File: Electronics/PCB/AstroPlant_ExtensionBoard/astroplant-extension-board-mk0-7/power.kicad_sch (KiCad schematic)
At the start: 13 parts, among them J14 61300621121, J20 Conn_01x02, J21 Conn_01x02

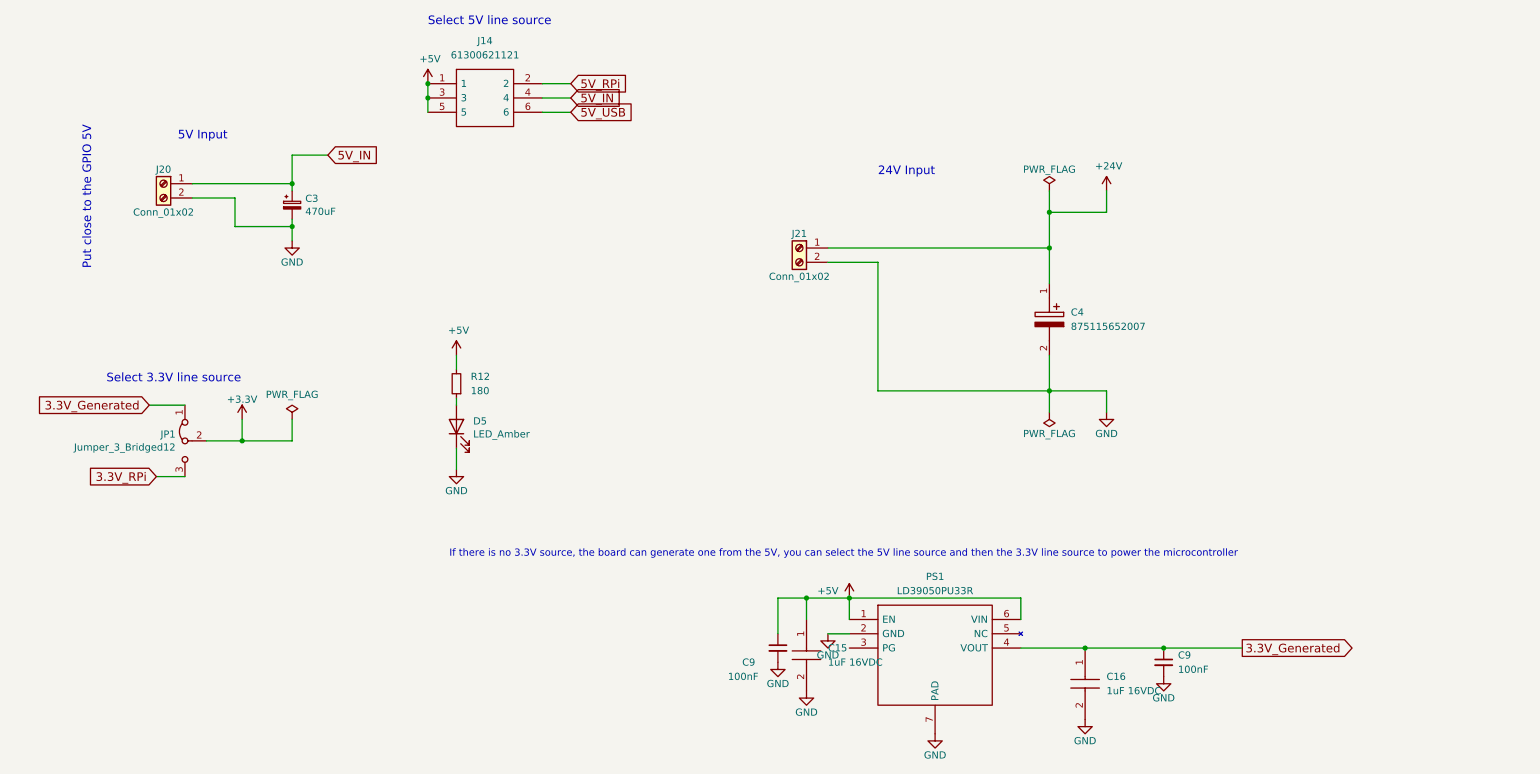
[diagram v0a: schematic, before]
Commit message: Updated PCB from a backup save, solve issues of the 1st prototype
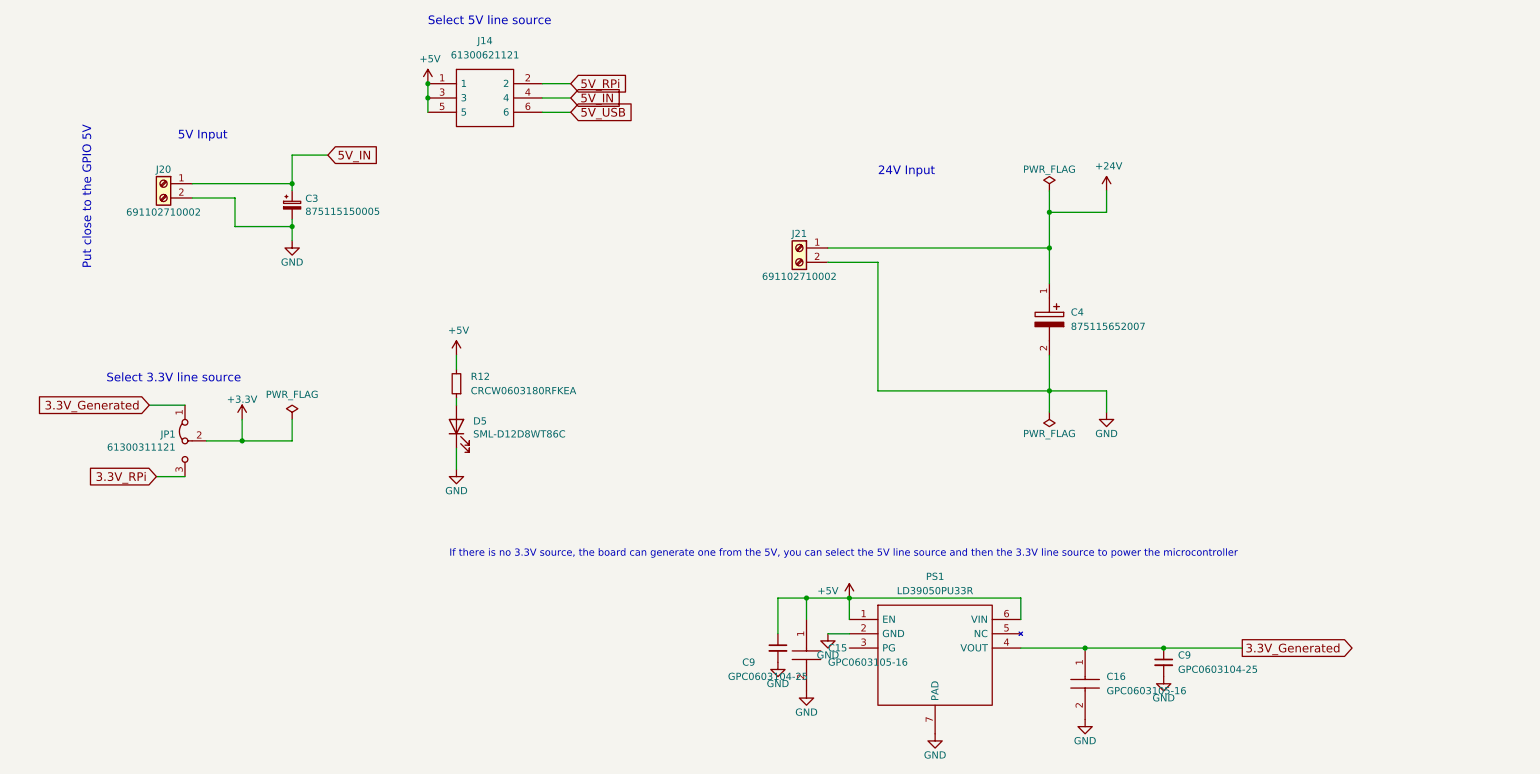
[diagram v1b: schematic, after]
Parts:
- C15, C16: value 1uF 16VDC -> GPC0603105-16; Capacitance (none) -> 1uF
- C3: value 470uF -> 875115150005; Capacitance (none) -> 470uF
- C4: Capacitance (none) -> 100uF
- C9: value 100nF -> GPC0603104-25; Capacitance (none) -> 100nF; MPN VJ0603Y104MXJCW1BC -> GPC0603104-25
- D5: value LED_Amber -> SML-D12D8WT86C; MPN SML-D12D8WT8 -> SML-D12D8WT86C; Manufacturer_Part_Number (none) -> SML-D12D8WT86C
- J20, J21: value Conn_01x02 -> 691102710002
- JP1: value Jumper_3_Bridged12 -> 61300311121
- R12: value 180 -> CRCW0603180RFKEA
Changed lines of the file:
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@@
       (effects (font (size 1.27 1.27)))
     )
-    (property "Value" "Conn_01x02" (at 179.07 78.74 0)
+    (property "Value" "691102710002" (at 179.07 78.74 0)
       (effects (font (size 1.27 1.27)))
     )
@@
       (effects (font (size 1.27 1.27)))
     )
-    (property "Value" "Conn_01x02" (at 66.04 67.31 0)
+    (property "Value" "691102710002" (at 66.04 67.31 0)
       (effects (font (size 1.27 1.27)))
     )
@@
       (effects (font (size 1.27 1.27)) (justify left))
     )
-    (property "Value" "470uF" (at 91.2368 67.183 0)
+    (property "Value" "875115150005" (at 91.2368 67.183 0)
       (effects (font (size 1.27 1.27)) (justify left))
     )
@@
     )
     (property "Digikey PN" "732-6443-1-ND" (at 88.9 66.04 0)
+      (effects (font (size 1.27 1.27)) hide)
+    )
+    (property "Capacitance" "470uF" (at 88.9 66.04 0)
       (effects (font (size 1.27 1.27)) hide)
     )
@@
       (effects (font (size 1.27 1.27)) (justify right))
     )
-    (property "Value" "LED_Amber" (at 121.0818 106.7562 90)
+    (property "Value" "SML-D12D8WT86C" (at 121.0818 106.7562 90)
       (effects (font (size 1.27 1.27)) (justify right))
     )
@@
       (effects (font (size 1.27 1.27)) hide)
     )
-    (property "MPN" "SML-D12D8WT8" (at 118.11 105.41 0)
+    (property "MPN" "SML-D12D8WT86C" (at 118.11 105.41 0)
       (effects (font (size 1.27 1.27)) hide)
     )
     (property "Mouser PN" " 755-SML-D12D8WT86C" (at 118.11 105.41 0)
+      (effects (font (size 1.27 1.27)) hide)
+    )
+    (property "Manufacturer_Part_Number" "SML-D12D8WT86C" (at 118.11 105.41 0)
       (effects (font (size 1.27 1.27)) hide)
     )
@@
       (effects (font (size 1.27 1.27)) hide)
     )
+    (property "Capacitance" "100uF" (at 223.52 80.01 0)
+      (effects (font (size 1.27 1.27)) hide)
+    )
     (pin "1")
     (pin "2")
@@
       (effects (font (size 1.27 1.27)) (justify left))
     )
-    (property "Value" "100nF" (at 246.38 148.5963 0)
+    (property "Value" "GPC0603104-25 " (at 246.38 148.5963 0)
       (effects (font (size 1.27 1.27)) (justify left))
     )
@@
       (effects (font (size 1.27 1.27)) hide)
     )
-    (property "MPN" "VJ0603Y104MXJCW1BC" (at 243.84 147.32 0)
+    (property "MPN" "GPC0603104-25 " (at 243.84 147.32 0)
+      (effects (font (size 1.27 1.27)) hide)
+    )
+    (property "Capacitance" "100nF" (at 243.84 147.32 0)
       (effects (font (size 1.27 1.27)) hide)
     )
@@
       (effects (font (size 1.27 1.27)) (justify left))
     )
-    (property "Value" "Jumper_3_Bridged12" (at 68.1736 109.093 90)
+    (property "Value" "61300311121" (at 68.1736 109.093 90)
       (effects (font (size 1.27 1.27)) (justify left))
     )
@@
       (effects (font (size 1.27 1.27)) (justify left))
     )
-    (property "Value" "1uF 16VDC" (at 233.68 152.4 90)
+    (property "Value" "GPC0603105-16" (at 233.68 152.4 90)
       (effects (font (size 1.27 1.27)) (justify left))
     )
@@
     (property "Arrow Price/Stock" "https://www.arrow.com/en/products/grm185r61c105ke44d/murata-manufacturing" (at 208.28 153.67 0)
       (effects (font (size 1.27 1.27)) (justify left) hide)
+    )
+    (property "Capacitance" "1uF" (at 229.87 144.78 0)
+      (effects (font (size 1.27 1.27)) hide)
     )
     (pin "1")
@@
       (effects (font (size 1.27 1.27)) (justify right))
     )
-    (property "Value" "180" (at 120.65 99.06 0)
+    (property "Value" "CRCW0603180RFKEA" (at 120.65 99.06 0)
       (effects (font (size 1.27 1.27)) (justify right))
     )
@@
       (effects (font (size 1.27 1.27)) (justify left))
     )
-    (property "Value" "100nF" (at 166.37 149.86 0)
+    (property "Value" "GPC0603104-25 " (at 166.37 149.86 0)
       (effects (font (size 1.27 1.27)) (justify left))
     )
@@
       (effects (font (size 1.27 1.27)) hide)
     )
-    (property "MPN" "VJ0603Y104MXJCW1BC" (at 175.26 144.78 0)
+    (property "MPN" "GPC0603104-25 " (at 175.26 144.78 0)
+      (effects (font (size 1.27 1.27)) hide)
+    )
+    (property "Capacitance" "100nF" (at 175.26 144.78 0)
       (effects (font (size 1.27 1.27)) hide)
     )
@@
       (effects (font (size 1.27 1.27)) (justify left))
     )
-    (property "Value" "1uF 16VDC" (at 184.15 147.32 90)
+    (property "Value" "GPC0603105-16" (at 184.15 147.32 90)
       (effects (font (size 1.27 1.27)) (justify left))
     )
@@
       (effects (font (size 1.27 1.27)) (justify left) hide)
     )
-    (pin "1")
+    (property "Capacitance" "1uF" (at 180.34 139.7 0)
+      (effects (font (size 1.27 1.27)) hide)
+    )
+    (pin "1")
